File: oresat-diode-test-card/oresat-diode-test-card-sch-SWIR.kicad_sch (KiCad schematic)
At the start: 29 parts, among them Q3 NMOS, Q4 DMP3050LVT-7, U4 TLV6001DCK, U501 TLV6001DCK, U8 NX3L4051-Q100, U9 TLV6001DCK

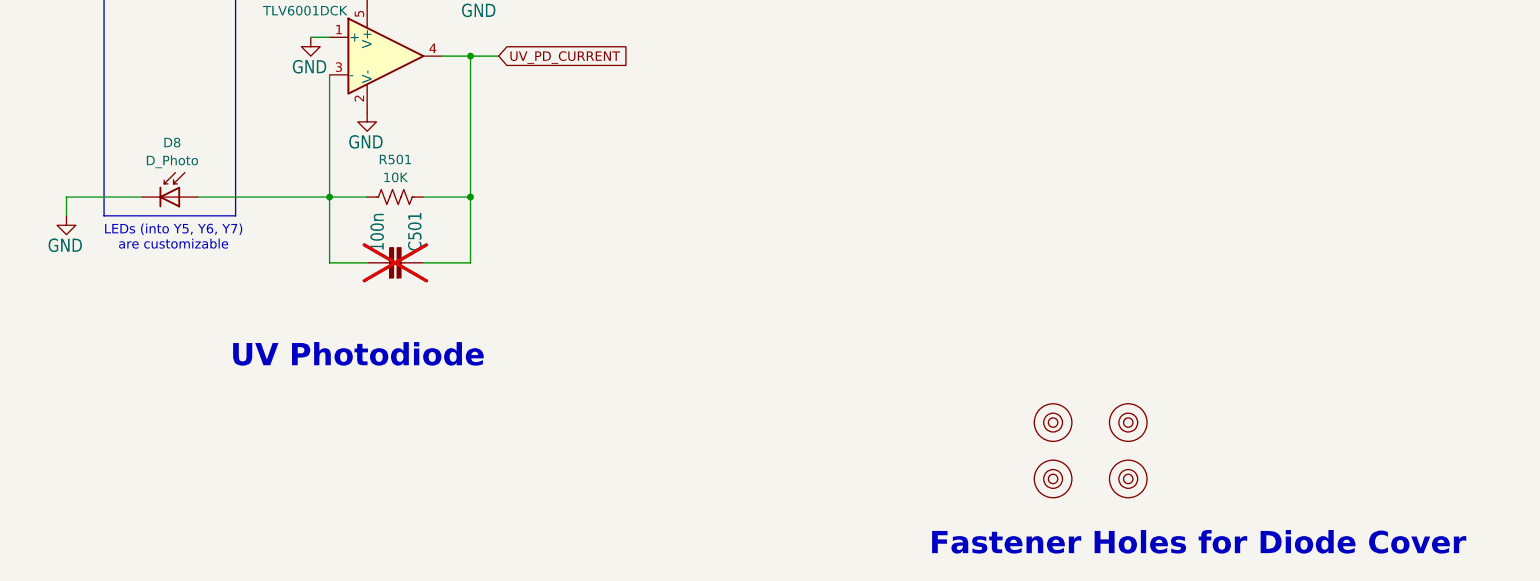
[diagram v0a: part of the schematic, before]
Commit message: second rought draft layout, fixed library issues
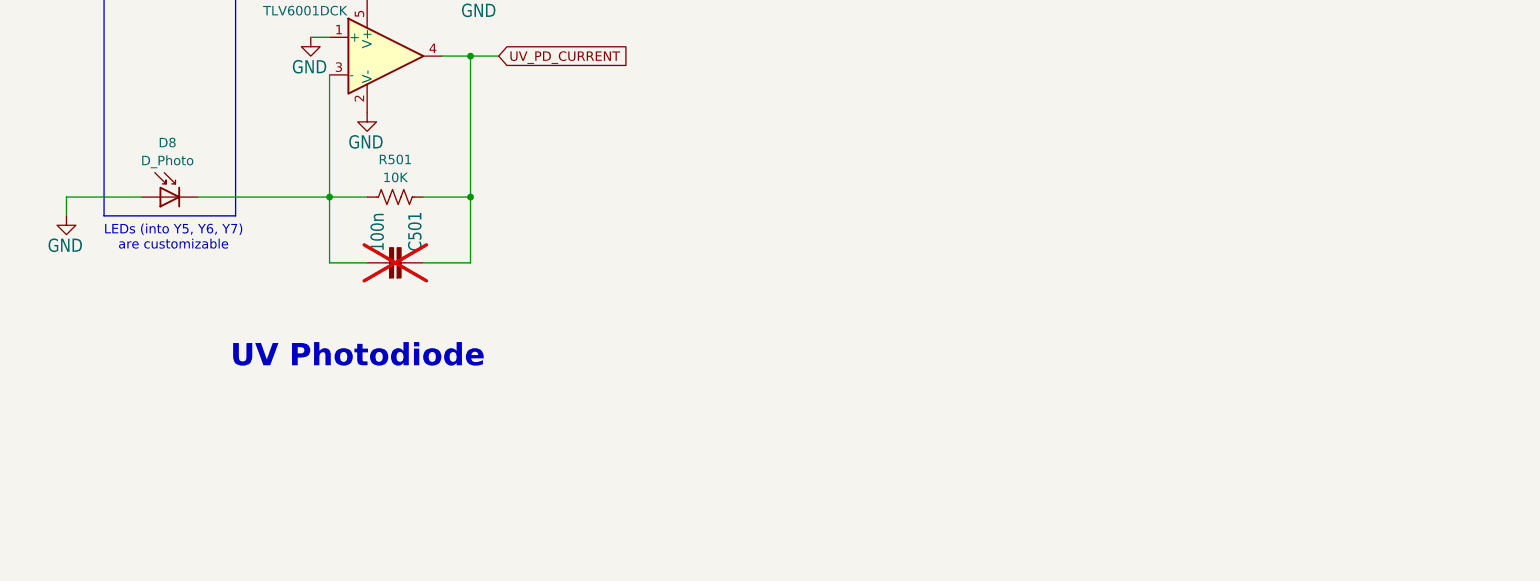
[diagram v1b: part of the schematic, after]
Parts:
- removed HW1, HW2, HW3, HW4: M2-Press-Fit-Nut, oresat-misc:M2-Press-Fit-Nut, symbol oresat-misc:M2-Press-Fit-Nut
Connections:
- net GND: now also D8.2 (A); no longer D8.1 (K)
- net at C501.2, R501.1, U501.3 (-): now also D8.1 (K); no longer D8.2 (A)
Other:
- note removed: "Fastener Holes for Diode Cover"

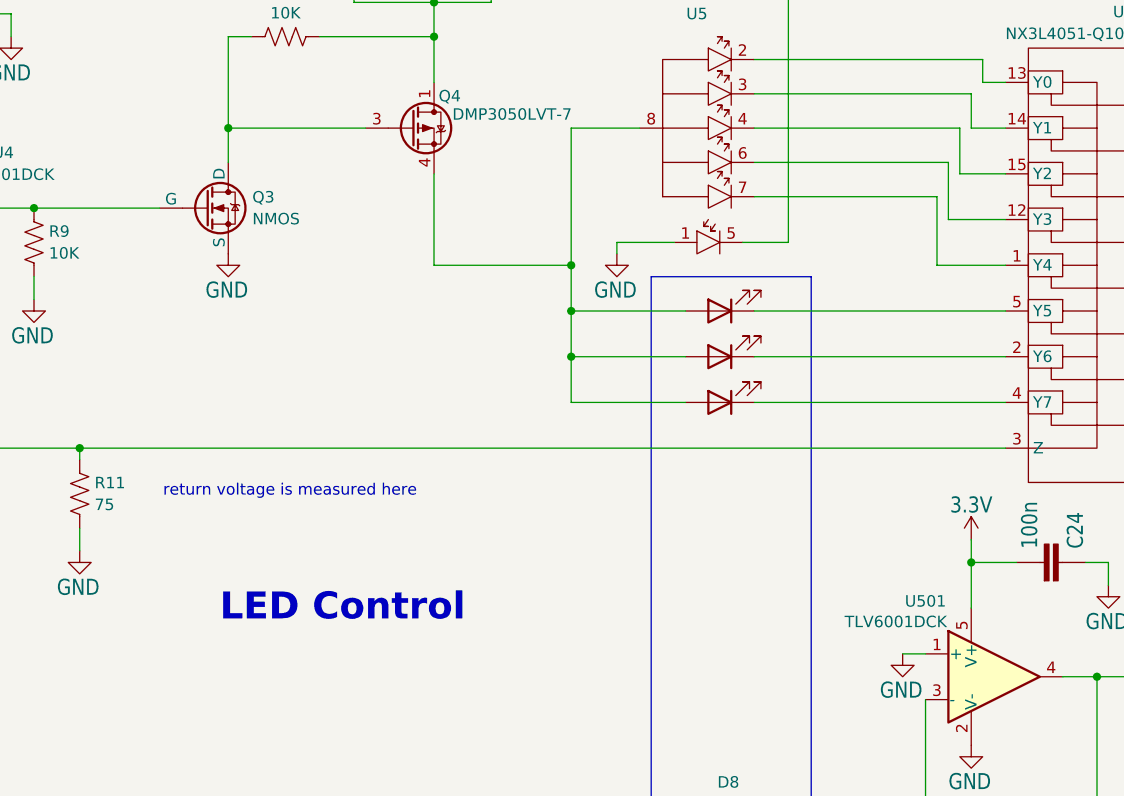
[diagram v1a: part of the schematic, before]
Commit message: Clean up of EAGLE imported ICs, added build directory, moved and locked diode hats.
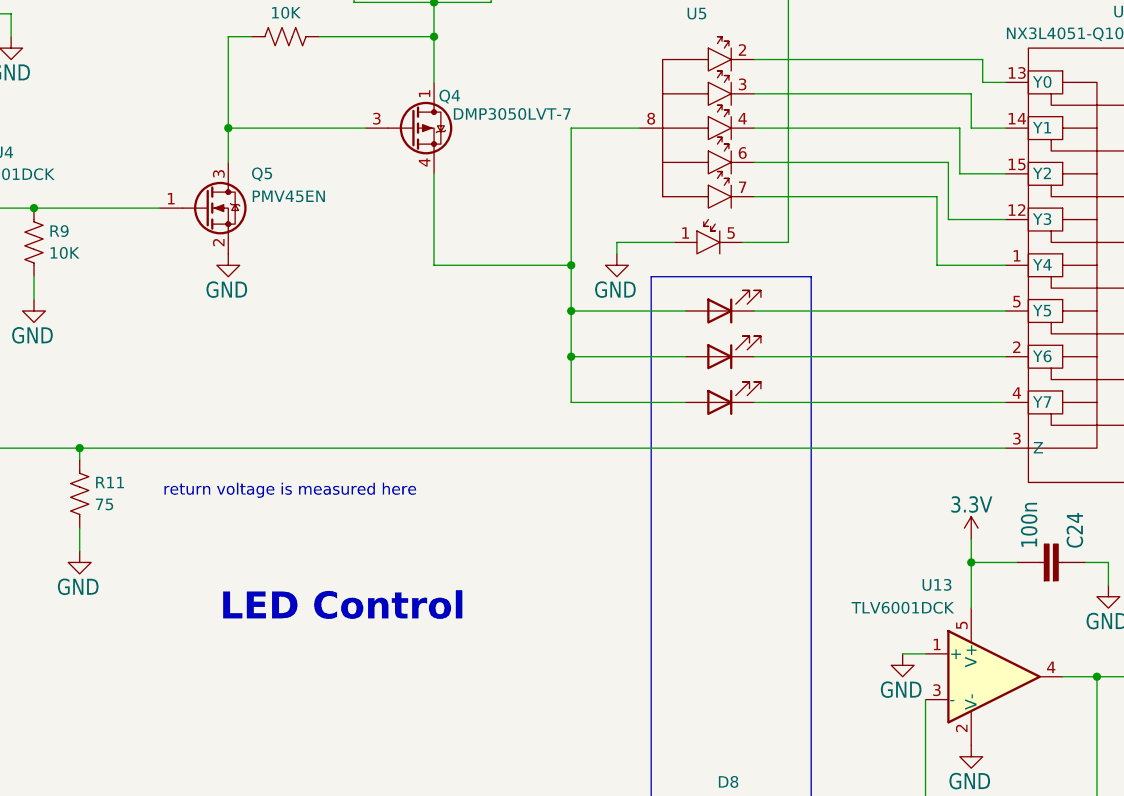
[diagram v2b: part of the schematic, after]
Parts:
- removed Q3: NMOS, Package_TO_SOT_SMD:SOT-23-6, symbol Simulation_SPICE:NMOS
- added Q5: PMV45EN, Package_TO_SOT_SMD:SOT-23-3, symbol Device:Q_NMOS_GSD
- renumbered U501 to U13
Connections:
- net GND: now also Q5.2 (S)
- net at Q4.3 (G), R8.1: now also Q5.3 (D)
- net at R9.2, U4.4: now also Q5.1 (G)
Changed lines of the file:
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@@
-	)
-	(symbol
-		(lib_id "Simulation_SPICE:NMOS")
-		(at 171.45 133.35 0)
-		(unit 1)
-		(exclude_from_sim no)
-		(in_bom yes)
-		(on_board yes)
-		(dnp no)
-		(fields_autoplaced yes)
-		(property "Reference" "Q3"
-			(at 176.657 132.1378 0)
-			(effects
-				(font
-					(size 1.27 1.27)
-				)
-				(justify left)
-			)
-		)
-		(property "Value" "NMOS"
-			(at 176.657 134.5621 0)
-			(effects
-				(font
-					(size 1.27 1.27)
-				)
-				(justify left)
-			)
-		)
-		(property "Footprint" "Package_TO_SOT_SMD:SOT-23-6"
-			(at 176.53 130.81 0)
-			(effects
-				(font
-					(size 1.27 1.27)
-				)
-				(hide yes)
-			)
-		)
-		(property "Datasheet" "https://ngspice.sourceforge.io/docs/ngspice-html-manual/manual.xhtml#cha_MOSFETs"
-			(at 171.45 146.05 0)
-			(effects
-				(font
-					(size 1.27 1.27)
-				)
-				(hide yes)
-			)
-		)
-		(property "Description" "N-MOSFET transistor, drain/source/gate"
-			(at 171.45 133.35 0)
-			(effects
-				(font
-					(size 1.27 1.27)
-				)
-				(hide yes)
-			)
-		)
-		(property "Sim.Device" "NMOS"
-			(at 171.45 150.495 0)
-			(effects
-				(font
-					(size 1.27 1.27)
-				)
-				(hide yes)
-			)
-		)
-		(property "Sim.Type" "VDMOS"
-			(at 171.45 152.4 0)
-			(effects
-				(font
-					(size 1.27 1.27)
-				)
-				(hide yes)
-			)
-		)
-		(property "Sim.Pins" "1=D 2=G 3=S"
-			(at 171.45 148.59 0)
-			(effects
-				(font
-					(size 1.27 1.27)
-				)
-				(hide yes)
-			)
-		)
-		(pin "1"
-		)
-		(pin "2"
-		)
-		(pin "3"
-		)
-		(instances
-			(project "oresat-diode-test-card"
-				(path "/04d32576-d084-475b-9eac-d7f3fd9579d7/a25fadb6-76d8-445f-be27-cd15465f11e4"
-					(reference "Q3")
-					(unit 1)
-				)
-			)
-		)
 	)
 	(symbol
@@
 		(on_board yes)
 		(dnp no)
-		(property "Reference" "U501"
-			(at 251.46 177.038 0)
+		(property "Reference" "U13"
+			(at 252.73 175.26 0)
 			(effects
 				(font
@@
 		)
 		(property "Value" "TLV6001DCK"
-			(at 248.158 179.324 0)
+			(at 248.92 177.8 0)
 			(effects
 				(font
@@
 			(project "oresat-diode-test-card"
 				(path "/04d32576-d084-475b-9eac-d7f3fd9579d7/a25fadb6-76d8-445f-be27-cd15465f11e4"
-					(reference "U501")
+					(reference "U13")
 					(unit 1)
 				)
@@
 	)
 	(symbol
+		(lib_id "Device:Q_NMOS_GSD")
+		(at 171.45 133.35 0)
+		(unit 1)
+		(exclude_from_sim no)
+		(in_bom yes)
+		(on_board yes)
+		(dnp no)
+		(property "Reference" "Q5"
+			(at 176.53 129.54 0)
+			(effects
+				(font
+					(size 1.27 1.27)
+				)
+				(justify left)
+			)
+		)
+		(property "Value" "PMV45EN"
+			(at 176.53 132.08 0)
+			(effects
+				(font
+					(size 1.27 1.27)
+				)
+				(justify left)
+			)
+		)
+		(property "Footprint" "Package_TO_SOT_SMD:SOT-23-3"
+			(at 176.53 130.81 0)
+			(effects
+				(font
+					(size 1.27 1.27)
+				)
+				(hide yes)
+			)
+		)
+		(property "Datasheet" "~"
+			(at 171.45 133.35 0)
+			(effects
+				(font
+					(size 1.27 1.27)
+				)
+				(hide yes)
+			)
+		)
+		(property "Description" "N-Channel 30V 4.1A (Ta) 510mW (Ta), 5W (Tc) Surface Mount TO-236AB"
+			(at 171.45 133.35 0)
+			(effects
+				(font
+					(size 1.27 1.27)
+				)
+				(hide yes)
+			)
+		)
+		(property "DPN" "1727-2307-1-ND"
+			(at 171.45 133.35 0)
+			(effects
+				(font
+					(size 1.27 1.27)
+				)
+				(hide yes)
+			)
+		)
+		(property "DST" "Digi-Key"
+			(at 171.45 133.35 0)
+			(effects
+				(font
+					(size 1.27 1.27)
+				)
+				(hide yes)
+			)
+		)
+		(property "MFR" "Nexperia"
+			(at 171.45 133.35 0)
+			(effects
+				(font
+					(size 1.27 1.27)
+				)
+				(hide yes)
+			)
+		)
+		(property "MPN" "PMV45EN2R"
+			(at 171.45 133.35 0)
+			(effects
+				(font
+					(size 1.27 1.27)
+				)
+				(hide yes)
+			)
+		)
+		(pin "1"
+		)
+		(pin "2"
+		)
+		(pin "3"
+		)
+		(instances
+			(project "oresat-diode-test-card"
+				(path "/04d32576-d084-475b-9eac-d7f3fd9579d7/a25fadb6-76d8-445f-be27-cd15465f11e4"
+					(reference "Q5")
+					(unit 1)
+				)
+			)
+		)
+	)
+	(symbol
 		(lib_id "oresat-proto-card-eagle-import:C-EU0603-C-NOSILK")
 		(at 266.7 172.72 270)
@@
 		(pin "11"
 		)
+		(pin "7"
+		)
 		(instances
 			(project "oresat-diode-test-card"
@@
 		(on_board yes)
 		(dnp no)
+		(fields_autoplaced yes)
 		(property "Reference" "U9"
 			(at 263.144 51.054 0)

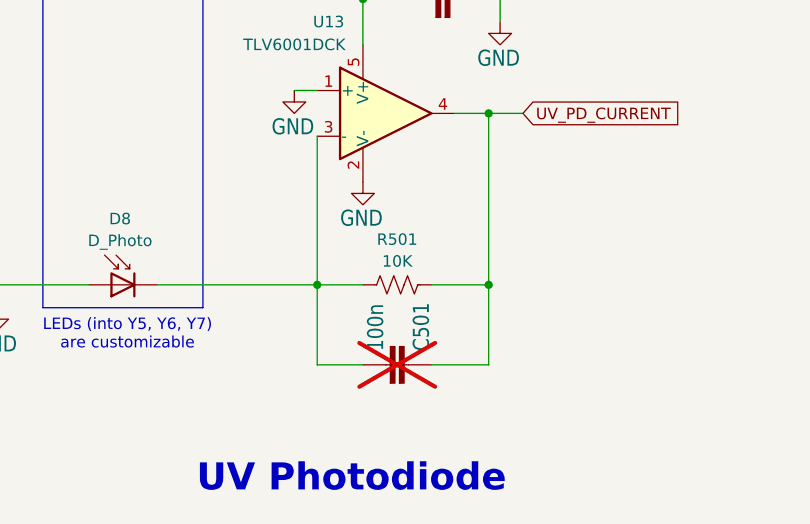
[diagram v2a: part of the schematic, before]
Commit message: Fix DRCs, clean up some routing, fix footprint movement on OPD.
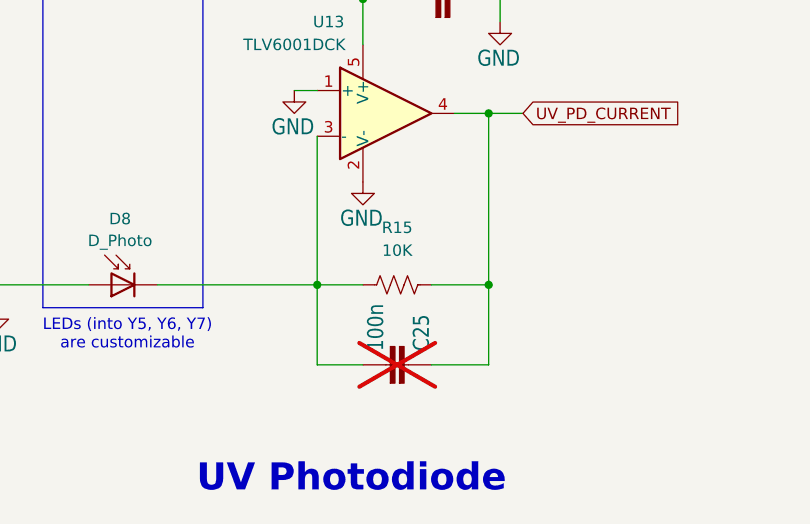
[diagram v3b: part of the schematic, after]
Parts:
- renumbered C501 to C25, R501 to R15
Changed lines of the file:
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@@
 		(on_board yes)
 		(dnp yes)
-		(property "Reference" "C501"
+		(property "Reference" "C25"
 			(at 262.001 211.836 0)
 			(effects
@@
 			(project "oresat-diode-test-card"
 				(path "/04d32576-d084-475b-9eac-d7f3fd9579d7/a25fadb6-76d8-445f-be27-cd15465f11e4"
-					(reference "C501")
+					(reference "C25")
 					(unit 1)
 				)
@@
 		(dnp no)
 		(fields_autoplaced yes)
-		(property "Reference" "R501"
-			(at 260.35 199.4365 90)
+		(property "Reference" "R15"
+			(at 260.35 198.12 90)
 			(effects
 				(font
@@
 		)
 		(property "Value" "10K"
-			(at 260.35 201.8608 90)
+			(at 260.35 200.66 90)
 			(effects
 				(font
@@
 			(project "oresat-diode-test-card"
 				(path "/04d32576-d084-475b-9eac-d7f3fd9579d7/a25fadb6-76d8-445f-be27-cd15465f11e4"
-					(reference "R501")
+					(reference "R15")
 					(unit 1)
 				)

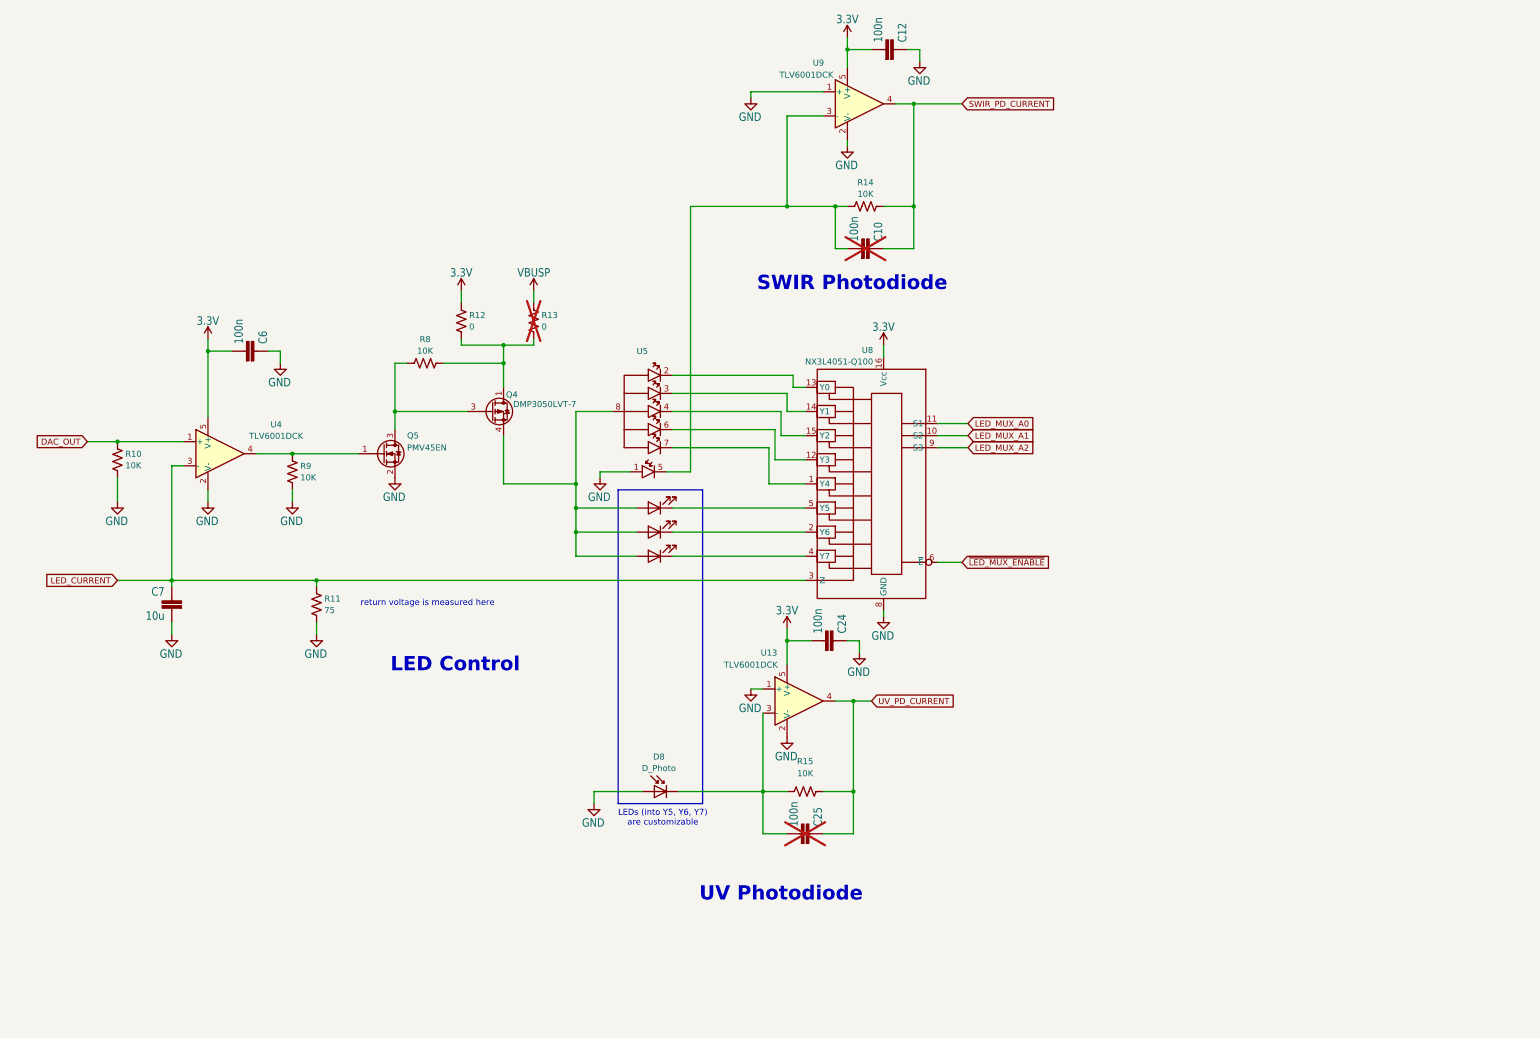
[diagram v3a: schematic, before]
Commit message: added test points and trace width edits
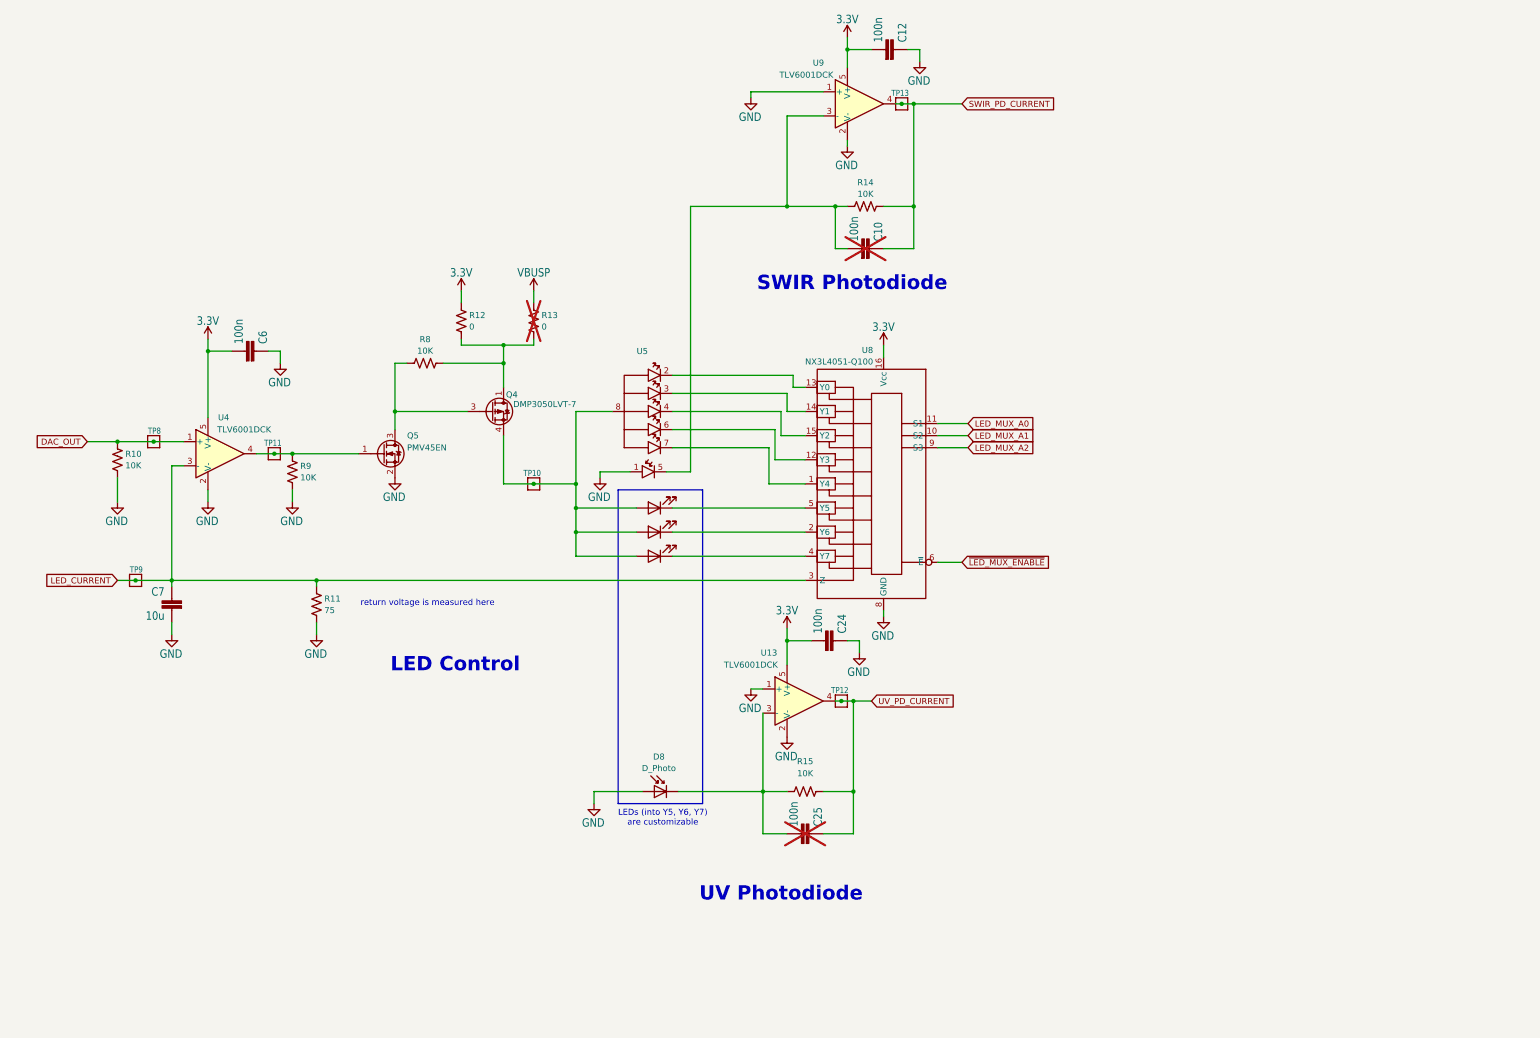
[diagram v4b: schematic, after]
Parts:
- added TP10, TP11, TP12, TP13, TP8, TP9: TEST-POINT-LARGE-SQUARE, oresat-proto-card:1X01, symbol oresat-proto-card-eagle-import:TEST-POINT-LARGE-SQUARE
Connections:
- net DAC_OUT: now also TP8.1
- net LED_CURRENT: now also TP9.1
- net SWIR_PD_CURRENT: now also TP13.1
- net UV_PD_CURRENT: now also TP12.1
- net at Q5.1 (G), R9.2, U4.4: now also TP11.1
- net at D1.2 (A), D2.2 (A), D4.2 (A)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: now also TP10.1
